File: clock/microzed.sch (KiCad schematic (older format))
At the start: 14 parts, among them P401 CONN_01X10, U401 74LVC541

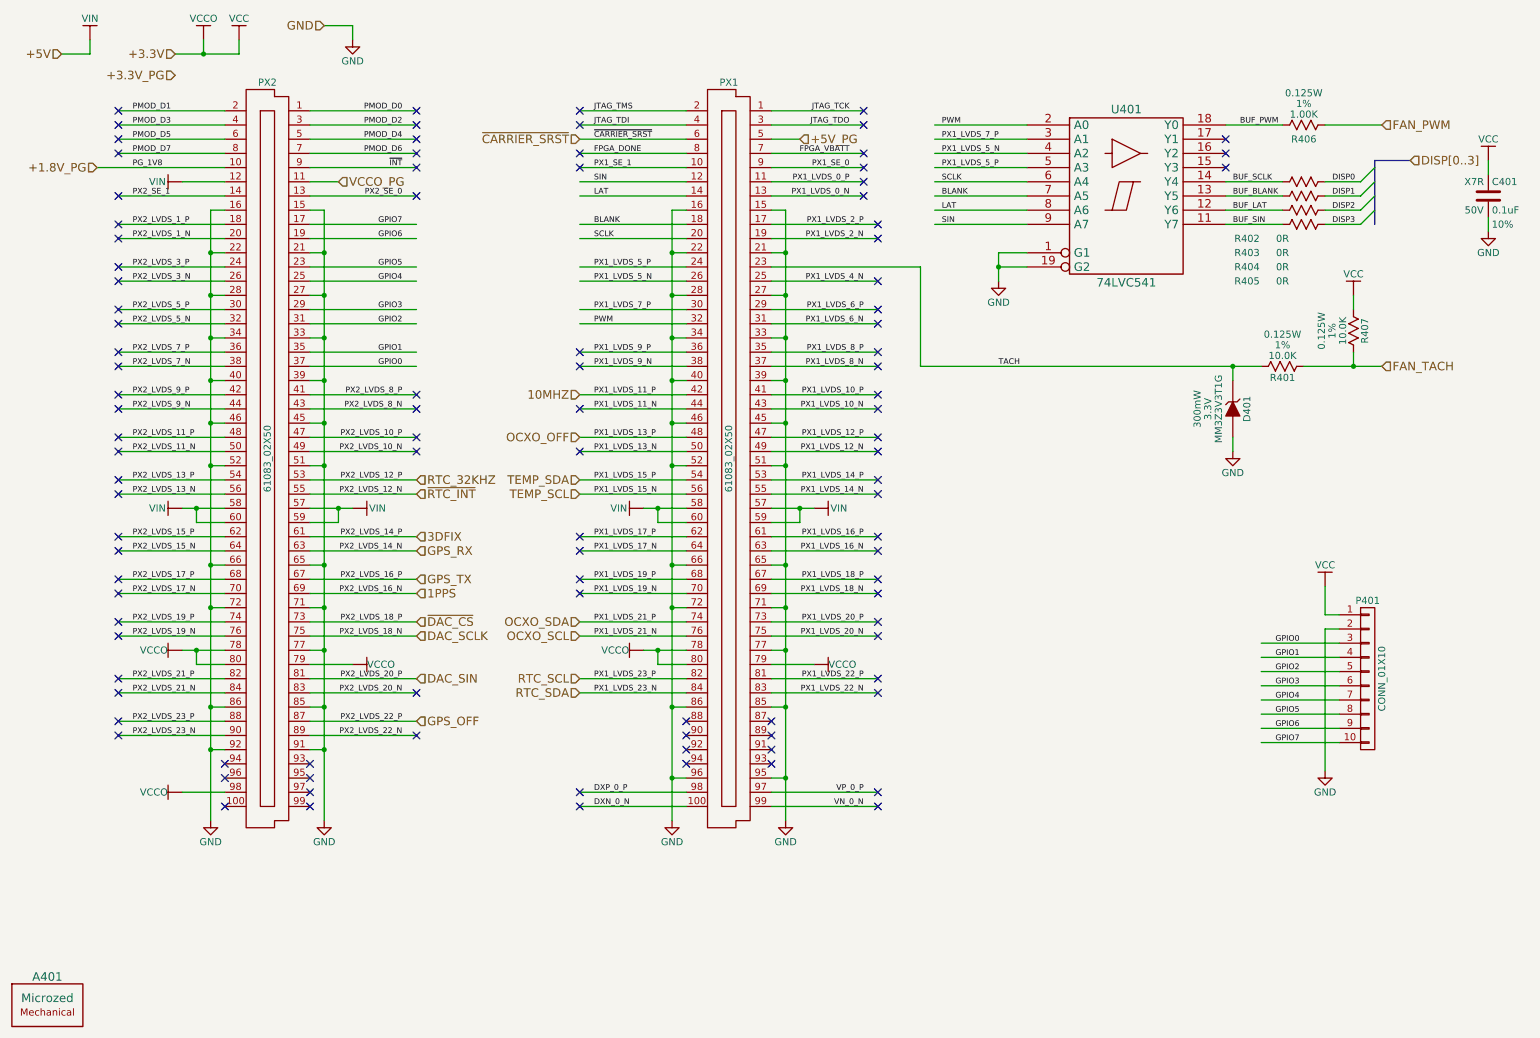
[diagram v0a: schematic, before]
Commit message: Start next revision of the main board. Power sequencing and control changes.
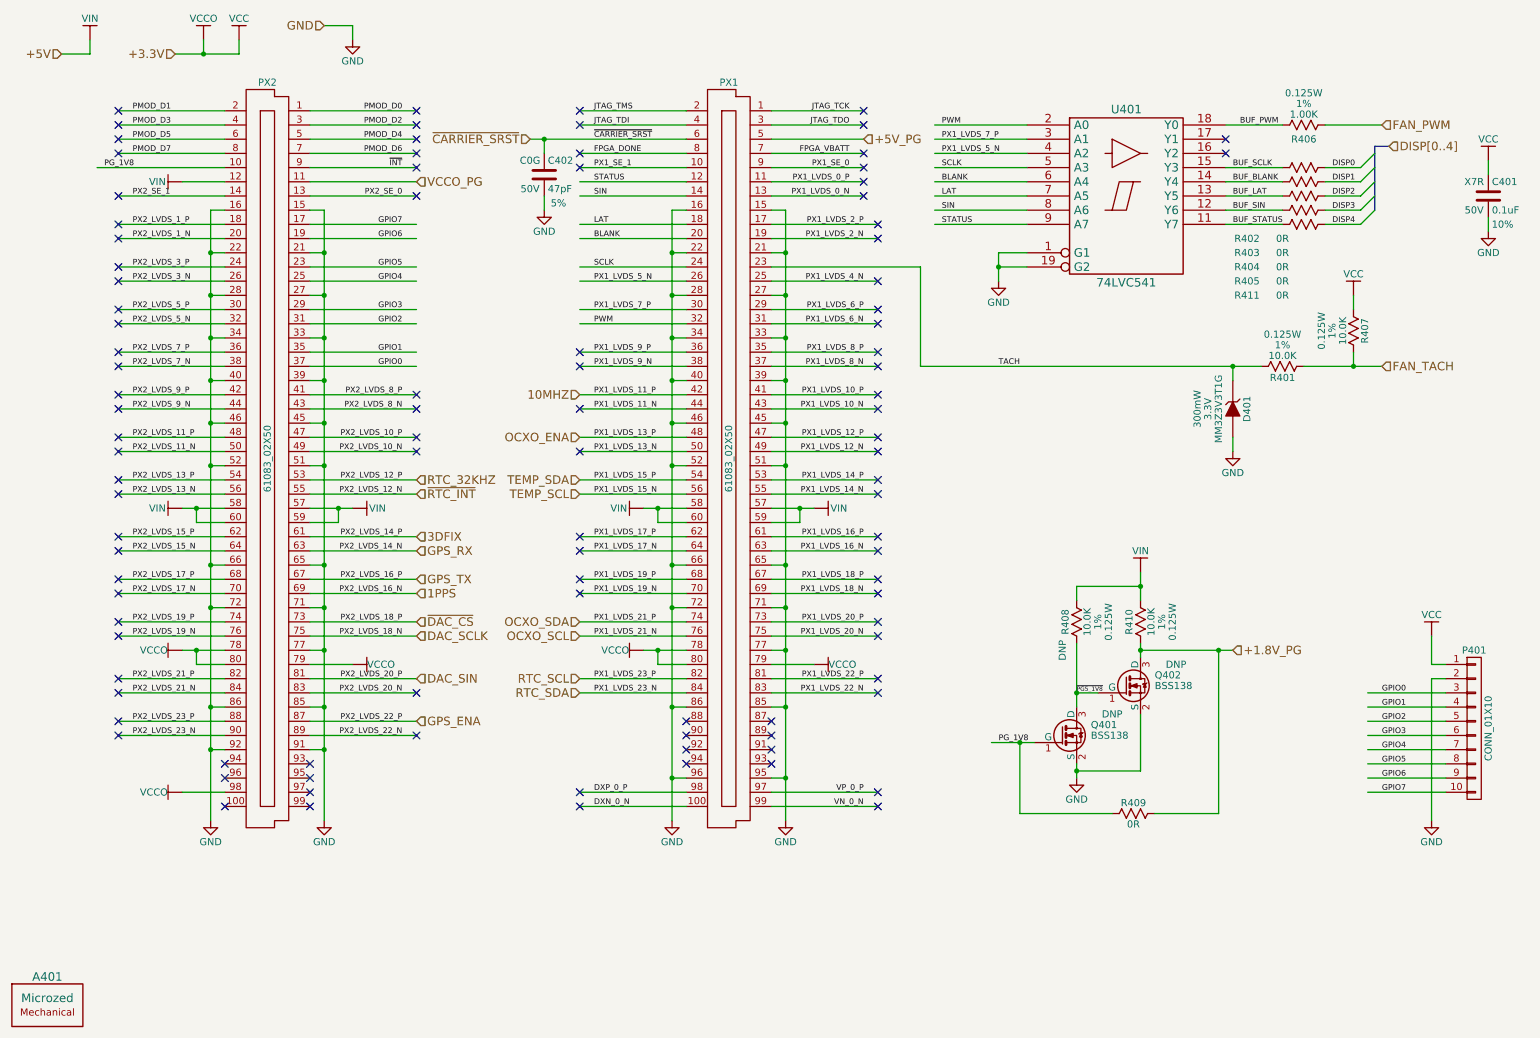
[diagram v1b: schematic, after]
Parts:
- added C402: 47pF, Capacitors_SMD:C_0805_HandSoldering, symbol C
- added Q401, Q402: BSS138, local:SOT-23-3_NXP_HandSoldering, symbol BSS138
- added R408, R410: 10.0K, Resistors_SMD:R_0805_HandSoldering, symbol R_local
- added R409, R411: 0R, Resistors_SMD:R_0805_HandSoldering, symbol R_local
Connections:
- net labels added: BUF_STATUS, DISP4, DISP[0..4], GPS_ENA, OCXO_ENA, STATUS, ~PG5_1V8~
- net labels removed: +3.3V_PG, DISP[0..3], GPS_OFF, OCXO_OFF, PX1_LVDS_5_P
- wire segments 244 -> 263
- no-connect marks 102 -> 101
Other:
- moved on the sheet: P401, R402, R403, R404, R405

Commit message: Checkpoint layout. Update hand soldering footprints for 0805 parts.
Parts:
- C401, C402: footprint Capacitors_SMD:C_0805_HandSoldering -> local:C_0805_HandSoldering
- D401: footprint local:SOD-323_477-02-H -> local:SOD-323_477-02-H_HandSoldering
- R401, R402, R403, R404, R405, R406, R407, R408, R409, R410, R411: footprint Resistors_SMD:R_0805_HandSoldering -> local:R_0805_HandSoldering

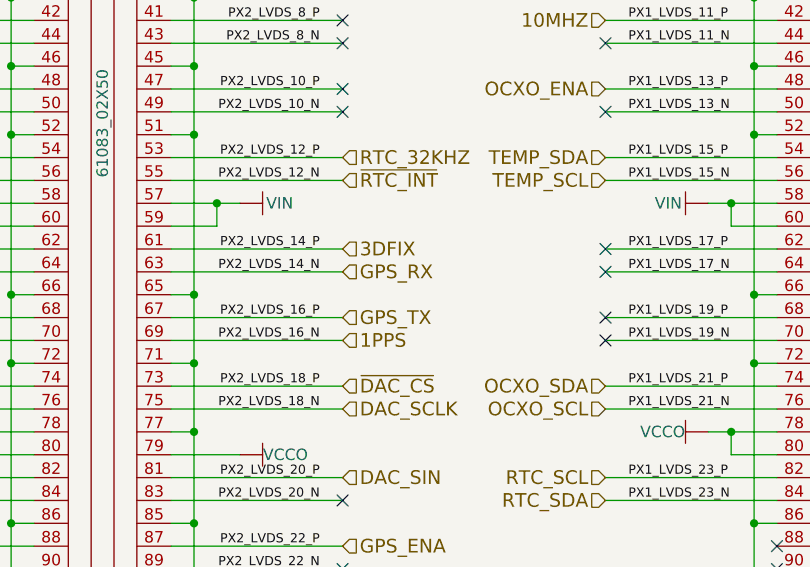
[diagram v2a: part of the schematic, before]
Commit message: Checkpoint layout. Change SOT-23-5 to hand soldering version.
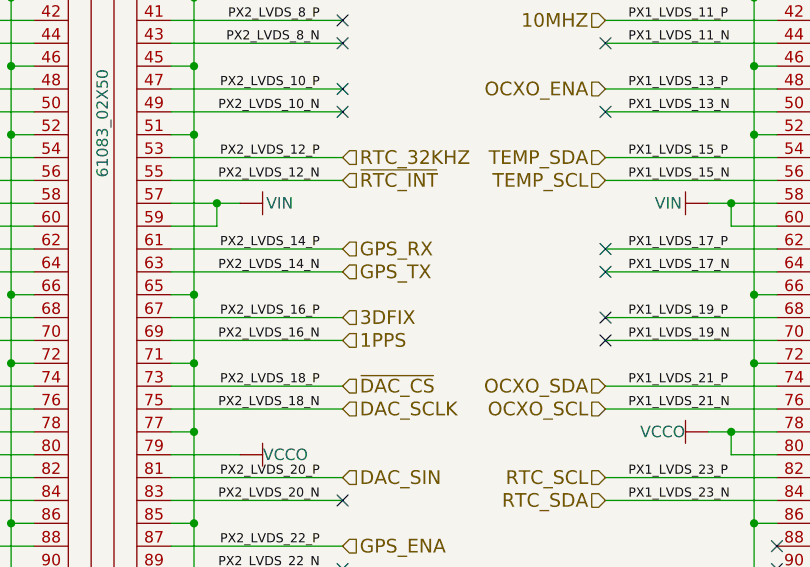
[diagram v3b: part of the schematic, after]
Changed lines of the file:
@@
 Text HLabel 3400 1750 2    60   Input ~ 0
 VCCO_PG
+Text HLabel 3400 4250 2    60   Input ~ 0
+GPS_RX
 Text HLabel 3400 4350 2    60   Input ~ 0
-GPS_RX
-Text HLabel 3400 4550 2    60   Input ~ 0
 GPS_TX
 Text HLabel 4550 4950 0    60   Input ~ 0
@@
 Text HLabel 3400 4650 2    60   Input ~ 0
 1PPS
-Text HLabel 3400 4250 2    60   Input ~ 0
+Text HLabel 3400 4550 2    60   Input ~ 0
 3DFIX
 $Comp

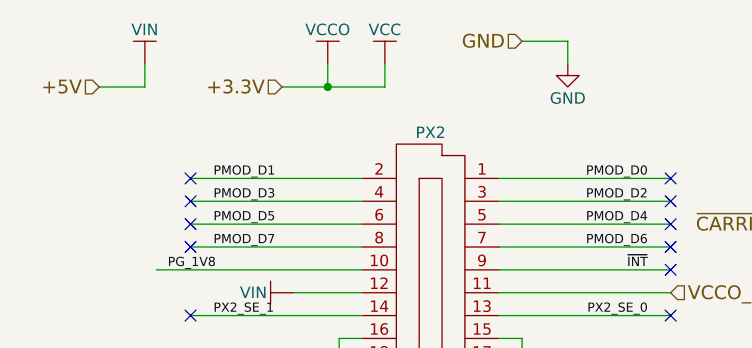
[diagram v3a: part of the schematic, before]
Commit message: Remove sheet to sheet power interconnect because power symbols are global.
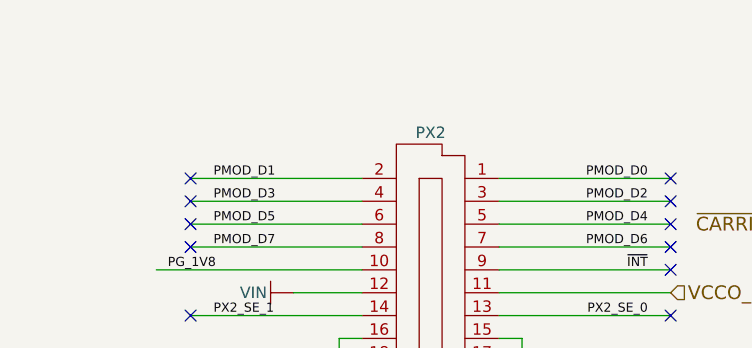
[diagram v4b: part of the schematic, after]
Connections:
- net labels removed: +3.3V, +5V
- wire segments 263 -> 256
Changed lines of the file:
@@
 $EndDescr
 $Comp
-L GND #PWR047
+L GND #PWR050
 U 1 1 5623DA38
 P 2750 6250
-F 0 "#PWR047" H 2750 6000 50  0001 C CNN
+F 0 "#PWR050" H 2750 6000 50  0001 C CNN
 F 1 "GND" H 2750 6100 50  0000 C CNN
 F 2 "" H 2750 6250 60  0000 C CNN
@@
 $EndComp
 $Comp
-L GND #PWR048
+L GND #PWR051
 U 1 1 5623DA70
 P 1950 6250
-F 0 "#PWR048" H 1950 6000 50  0001 C CNN
+F 0 "#PWR051" H 1950 6000 50  0001 C CNN
 F 1 "GND" H 1950 6100 50  0000 C CNN
 F 2 "" H 1950 6250 60  0000 C CNN
@@
 $EndComp
 $Comp
-L GND #PWR049
+L GND #PWR052
 U 1 1 5623DAE1
 P 6000 6250
-F 0 "#PWR049" H 6000 6000 50  0001 C CNN
+F 0 "#PWR052" H 6000 6000 50  0001 C CNN
 F 1 "GND" H 6000 6100 50  0000 C CNN
 F 2 "" H 6000 6250 60  0000 C CNN
@@
 $EndComp
 $Comp
-L GND #PWR050
+L GND #PWR053
 U 1 1 5623DB66
 P 5200 6250
-F 0 "#PWR050" H 5200 6000 50  0001 C CNN
+F 0 "#PWR053" H 5200 6000 50  0001 C CNN
 F 1 "GND" H 5200 6100 50  0000 C CNN
 F 2 "" H 5200 6250 60  0000 C CNN
@@
 	2050 1750 1750 1750
 $Comp
-L VIN #PWR051
+L VIN #PWR054
 U 1 1 5623ED14
 P 1750 1750
-F 0 "#PWR051" H 1750 1600 50  0001 C CNN
+F 0 "#PWR054" H 1750 1600 50  0001 C CNN
 F 1 "VIN" V 1750 1925 50  0000 C CNN
 F 2 "" H 1750 1750 60  0000 C CNN
@@
 $EndComp
 $Comp
-L VIN #PWR052
+L VIN #PWR055
 U 1 1 5623ED8A
 P 1750 4050
-F 0 "#PWR052" H 1750 3900 50  0001 C CNN
+F 0 "#PWR055" H 1750 3900 50  0001 C CNN
 F 1 "VIN" V 1750 4225 50  0000 C CNN
 F 2 "" H 1750 4050 60  0000 C CNN
@@
 $EndComp
 $Comp
-L VIN #PWR053
+L VIN #PWR056
 U 1 1 5623EE30
 P 2950 4050
-F 0 "#PWR053" H 2950 3900 50  0001 C CNN
+F 0 "#PWR056" H 2950 3900 50  0001 C CNN
 F 1 "VIN" V 2950 4225 50  0000 C CNN
 F 2 "" H 2950 4050 60  0000 C CNN
@@
 $EndComp
 $Comp
-L VIN #PWR054
+L VIN #PWR057
 U 1 1 5623EEAF
 P 5000 4050
-F 0 "#PWR054" H 5000 3900 50  0001 C CNN
+F 0 "#PWR057" H 5000 3900 50  0001 C CNN
 F 1 "VIN" V 5000 4225 50  0000 C CNN
 F 2 "" H 5000 4050 60  0000 C CNN
@@
 $EndComp
 $Comp
-L VIN #PWR055
+L VIN #PWR058
 U 1 1 5623EF12
 P 6200 4050
-F 0 "#PWR055" H 6200 3900 50  0001 C CNN
+F 0 "#PWR058" H 6200 3900 50  0001 C CNN
 F 1 "VIN" V 6200 4225 50  0000 C CNN
 F 2 "" H 6200 4050 60  0000 C CNN
@@
 Connection ~ 5100 5050
 $Comp
-L VCCO #PWR056
+L VCCO #PWR059
 U 1 1 5623F518
 P 6200 5150
-F 0 "#PWR056" H 6200 5000 50  0001 C CNN
+F 0 "#PWR059" H 6200 5000 50  0001 C CNN
 F 1 "VCCO" V 6200 5350 50  0000 C CNN
 F 2 "" H 6200 5150 60  0000 C CNN
@@
 Connection ~ 1850 5050
 $Comp
-L VCCO #PWR057
+L VCCO #PWR060
 U 1 1 5623F63E
 P 1750 5050
-F 0 "#PWR057" H 1750 4900 50  0001 C CNN
+F 0 "#PWR060" H 1750 4900 50  0001 C CNN
 F 1 "VCCO" V 1750 5250 50  0000 C CNN
 F 2 "" H 1750 5050 60  0000 C CNN
@@
 	2650 5150 2950 5150
 $Comp
-L VCCO #PWR058
+L VCCO #PWR061
 U 1 1 5623F67B
 P 2950 5150
-F 0 "#PWR058" H 2950 5000 50  0001 C CNN
+F 0 "#PWR061" H 2950 5000 50  0001 C CNN
 F 1 "VCCO" V 2950 5350 50  0000 C CNN
 F 2 "" H 2950 5150 60  0000 C CNN
@@
 	2050 6050 1750 6050
 $Comp
-L VCCO #PWR059
+L VCCO #PWR062
 U 1 1 5623F755
 P 1750 6050
-F 0 "#PWR059" H 1750 5900 50  0001 C CNN
+F 0 "#PWR062" H 1750 5900 50  0001 C CNN
 F 1 "VCCO" V 1750 6250 50  0000 C CNN
 F 2 "" H 1750 6050 60  0000 C CNN
@@
 	0    -1   -1   0
 $EndComp
-Text HLabel 900  850  0    60   Input ~ 0
-+5V
-Text HLabel 1700 850  0    60   Input ~ 0
-+3.3V
-Text HLabel 2750 650  0    60   Input ~ 0
-GND
 Text HLabel 6550 1450 2    60   Input ~ 0
 +5V_PG
@@
 Text HLabel 3400 4550 2    60   Input ~ 0
 3DFIX
-$Comp
-L VIN #PWR060
-U 1 1 562597FE
-P 1100 750
-F 0 "#PWR060" H 1100 600 50  0001 C CNN
-F 1 "VIN" H 1100 900 50  0000 C CNN
-F 2 "" H 1100 750 60  0000 C CNN
-F 3 "" H 1100 750 60  0000 C CNN
-	1    1100 750
-	1    0    0    -1
-$EndComp
-Wire Wire Line
-	900  850  1100 850
-Wire Wire Line
-	1100 850  1100 750
-$Comp
-L VCCO #PWR061
-U 1 1 562598AE
-P 1900 750
-F 0 "#PWR061" H 1900 600 50  0001 C CNN
-F 1 "VCCO" H 1900 900 50  0000 C CNN
-F 2 "" H 1900 750 60  0000 C CNN
-F 3 "" H 1900 750 60  0000 C CNN
-	1    1900 750
-	1    0    0    -1
-$EndComp
-Wire Wire Line
-	1700 850  2150 850
-Wire Wire Line
-	1900 850  1900 750
-$Comp
-L GND #PWR062
-U 1 1 56259970
-P 2950 750
-F 0 "#PWR062" H 2950 500 50  0001 C CNN
-F 1 "GND" H 2950 600 50  0000 C CNN
-F 2 "" H 2950 750 60  0000 C CNN
-F 3 "" H 2950 750 60  0000 C CNN
-	1    2950 750
-	1    0    0    -1
-$EndComp
-Wire Wire Line
-	2950 750  2950 650
-Wire Wire Line
-	2950 650  2750 650
 Wire Wire Line
 	5900 1450 6550 1450
@@
 DISP3
 $Comp
-L VCC #PWR063
-U 1 1 56368B50
-P 2150 750
-F 0 "#PWR063" H 2150 600 50  0001 C CNN
-F 1 "VCC" H 2150 900 50  0000 C CNN
-F 2 "" H 2150 750 60  0000 C CNN
-F 3 "" H 2150 750 60  0000 C CNN
-	1    2150 750
-	1    0    0    -1
-$EndComp
-Wire Wire Line
-	2150 850  2150 750
-Connection ~ 1900 850
-$Comp
 L R_local R402
 U 1 1 563694E5
@@
 Connection ~ 7500 2350
 $Comp
-L GND #PWR064
+L GND #PWR063
 U 1 1 56369E58
 P 7500 2450
-F 0 "#PWR064" H 7500 2200 50  0001 C CNN
+F 0 "#PWR063" H 7500 2200 50  0001 C CNN
 F 1 "GND" H 7500 2300 50  0000 C CNN
 F 2 "" H 7500 2450 60  0000 C CNN
@@
 	9150 3050 9150 3150
 $Comp
-L VCC #PWR065
+L VCC #PWR064
 U 1 1 563911B0
 P 10000 2550
-F 0 "#PWR065" H 10000 2400 50  0001 C CNN
+F 0 "#PWR064" H 10000 2400 50  0001 C CNN
 F 1 "VCC" H 10000 2700 50  0000 C CNN
 F 2 "" H 10000 2550 60  0000 C CNN
@@
 $EndComp
 $Comp
-L GND #PWR066
+L GND #PWR065
 U 1 1 563911DC
 P 9150 3650
-F 0 "#PWR066" H 9150 3400 50  0001 C CNN
+F 0 "#PWR065" H 9150 3400 50  0001 C CNN
 F 1 "GND" H 9150 3500 50  0000 C CNN
 F 2 "" H 9150 3650 60  0000 C CNN
@@
 NoConn ~ 9100 1550
 $Comp
-L VCCO #PWR067
+L VCCO #PWR066
 U 1 1 563E2413
 P 5000 5050
-F 0 "#PWR067" H 5000 4900 50  0001 C CNN
+F 0 "#PWR066" H 5000 4900 50  0001 C CNN
 F 1 "VCCO" V 5000 5250 50  0000 C CNN
 F 2 "" H 5000 5050 60  0000 C CNN
@@
 TACH
 $Comp
-L GND #PWR068
+L GND #PWR067
 U 1 1 56403C33
 P 10950 2100
-F 0 "#PWR068" H 10950 1850 50  0001 C CNN
+F 0 "#PWR067" H 10950 1850 50  0001 C CNN
 F 1 "GND" H 10950 1950 50  0000 C CNN
 F 2 "" H 10950 2100 60  0000 C CNN
@@
 $EndComp
 $Comp
-L VCC #PWR069
+L VCC #PWR068
 U 1 1 56403C47
 P 10950 1600
-F 0 "#PWR069" H 10950 1450 50  0001 C CNN
+F 0 "#PWR068" H 10950 1450 50  0001 C CNN
 F 1 "VCC" H 10950 1750 50  0000 C CNN
 F 2 "" H 10950 1600 60  0000 C CNN
@@
 	10550 5150 10550 4950
 $Comp
-L VCC #PWR070
+L VCC #PWR069
 U 1 1 56982CA5
 P 10550 4950
-F 0 "#PWR070" H 10550 4800 50  0001 C CNN
+F 0 "#PWR069" H 10550 4800 50  0001 C CNN
 F 1 "VCC" H 10550 5100 50  0000 C CNN
 F 2 "" H 10550 4950 60  0000 C CNN
@@
 $EndComp
 $Comp
-L GND #PWR071
+L GND #PWR070
 U 1 1 56982CDA
 P 10550 6250
-F 0 "#PWR071" H 10550 6000 50  0001 C CNN
+F 0 "#PWR070" H 10550 6000 50  0001 C CNN
 F 1 "GND" H 10550 6100 50  0000 C CNN
 F 2 "" H 10550 6250 60  0000 C CNN
@@
 	8050 5850 8050 5950
 $Comp
-L GND #PWR072
+L GND #PWR071
 U 1 1 57B7BAC3
 P 8050 5950
-F 0 "#PWR072" H 8050 5700 50  0001 C CNN
+F 0 "#PWR071" H 8050 5700 50  0001 C CNN
 F 1 "GND" H 8050 5800 50  0000 C CNN
 F 2 "" H 8050 5950 60  0000 C CNN
@@
 Connection ~ 8500 4600
 $Comp
-L VIN #PWR073
+L VIN #PWR072
 U 1 1 57B7C8E7
 P 8500 4500
-F 0 "#PWR073" H 8500 4350 50  0001 C CNN
+F 0 "#PWR072" H 8500 4350 50  0001 C CNN
 F 1 "VIN" H 8500 4650 50  0000 C CNN
 F 2 "" H 8500 4500 60  0000 C CNN
@@
 $EndComp
 $Comp
-L GND #PWR074
+L GND #PWR073
 U 1 1 5858D873
 P 4300 1950
-F 0 "#PWR074" H 4300 1700 50  0001 C CNN
+F 0 "#PWR073" H 4300 1700 50  0001 C CNN
 F 1 "GND" H 4300 1800 50  0000 C CNN
 F 2 "" H 4300 1950 60  0000 C CNN

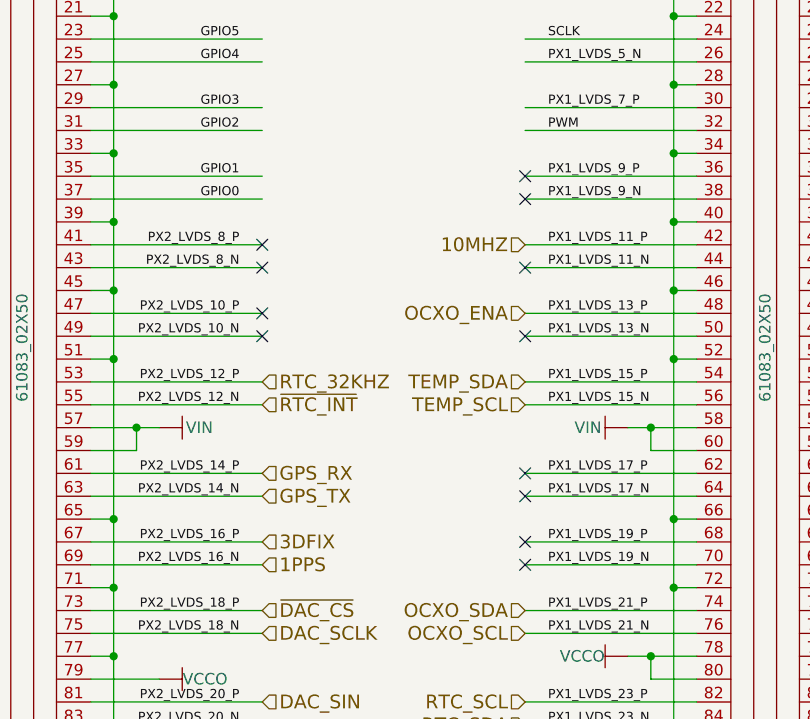
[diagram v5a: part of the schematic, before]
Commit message: Connect temperature sensor interrupt to FPGA.
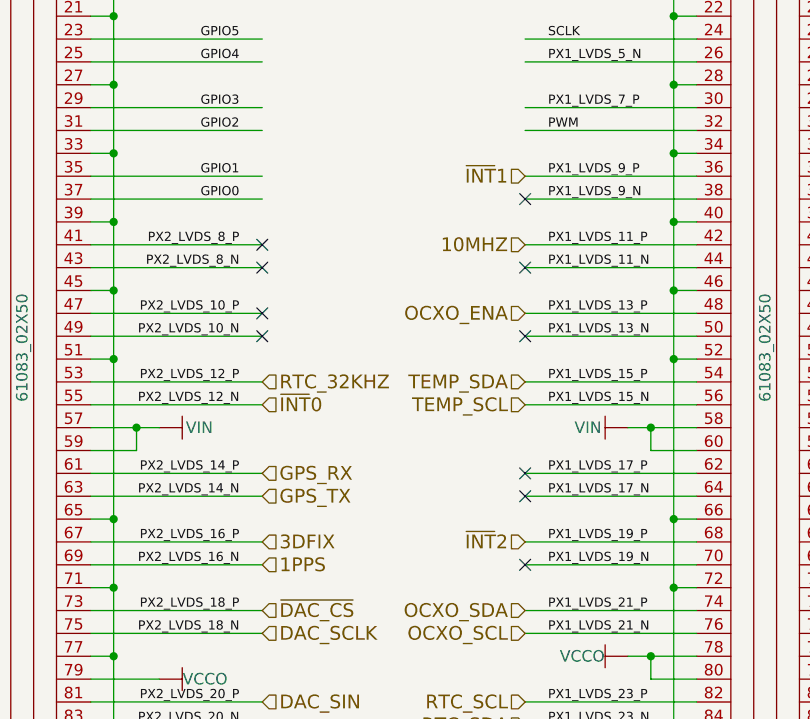
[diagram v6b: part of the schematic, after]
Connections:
- net labels added: ~INT~0, ~INT~1, ~INT~2
- net labels removed: ~RTC_INT~
- no-connect marks 101 -> 99
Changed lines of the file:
@@
 Text Label 3300 3850 2    40   ~ 0
 PX2_LVDS_12_P
-NoConn ~ 4550 4550
 Text Label 1400 3850 0    40   ~ 0
 PX2_LVDS_13_P
@@
 Text Label 4650 2950 0    40   ~ 0
 PX1_LVDS_9_P
-NoConn ~ 4550 2950
+NoConn ~ 4550 4250
 Wire Wire Line
 	5300 3350 4550 3350
@@
 Text Label 4650 4250 0    40   ~ 0
 PX1_LVDS_17_P
-NoConn ~ 4550 4250
 Wire Wire Line
 	5300 4650 4550 4650
@@
 RTC_32KHZ
 Text HLabel 3400 3950 2    60   Input ~ 0
-~RTC_INT~
+~INT~0
 NoConn ~ 6650 2050
 NoConn ~ 6650 2150
@@
 	0    1    1    0
 $EndComp
+Text HLabel 4550 2950 0    60   Input ~ 0
+~INT~1
+Text HLabel 4550 4550 0    60   Input ~ 0
+~INT~2
 $EndSCHEMATC
